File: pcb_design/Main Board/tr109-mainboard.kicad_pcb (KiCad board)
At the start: 2 copper layers, 60.3 x 60.4 mm, 23 parts, among them J1 Raspberry Pi Zero W, J2 ST7735_Screen, J3 Light_Board, J4 Cap_and_Bat, J5 Hall_1, J6 Audio_Out, J7 Hall_2, J8 Led_On, J9 i2c Connect, U1 CAP1208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

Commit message: Updated PCBs
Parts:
- added G***: Picorder Logo, Logos:Picorder Logo, F.Cu at (150.9, 101.0)
- J2: value ST7735_Screen -> ST7735 Screen
- moved J9 10.2 mm to (164.8, 110.9)
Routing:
- net SDA: track 94.4 -> 104.5 mm
- net SCL: track 90.5 -> 99.1 mm
- net 3v3: track 98.5 -> 106.2 mm
- net LED_ON: track 75.2 -> 76.4 mm
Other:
- board text added: "C.BARRETT 2025"
- board text added: "CAPACITIVE PADS"
- board text added: "GNDN"
- board text added: "H2"
- board text added: "HALL SENSOR 2"
- board text added: "STATUS"
- board text removed: "CAPACITIVE BUTTONS"
- board text removed: "GNDN 47"
- board text removed: "LOW"

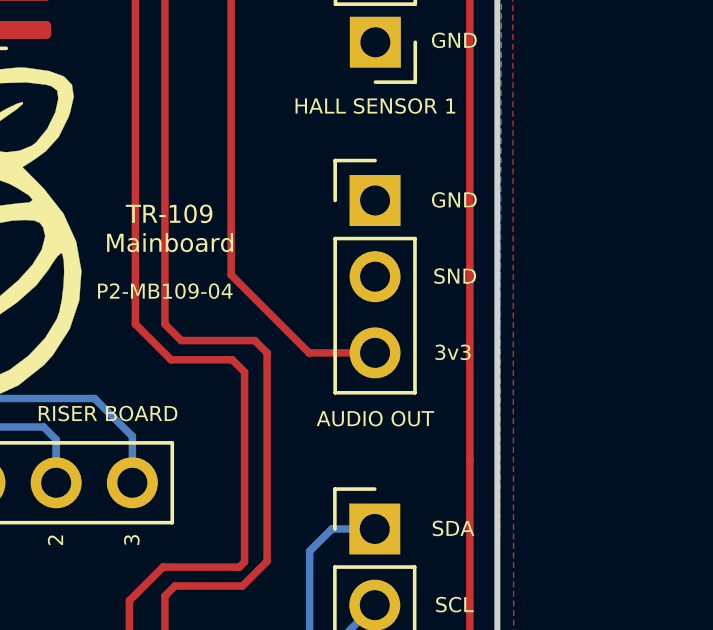
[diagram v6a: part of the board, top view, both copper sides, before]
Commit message: Fixed some kicad PCB errors, updated Blender file
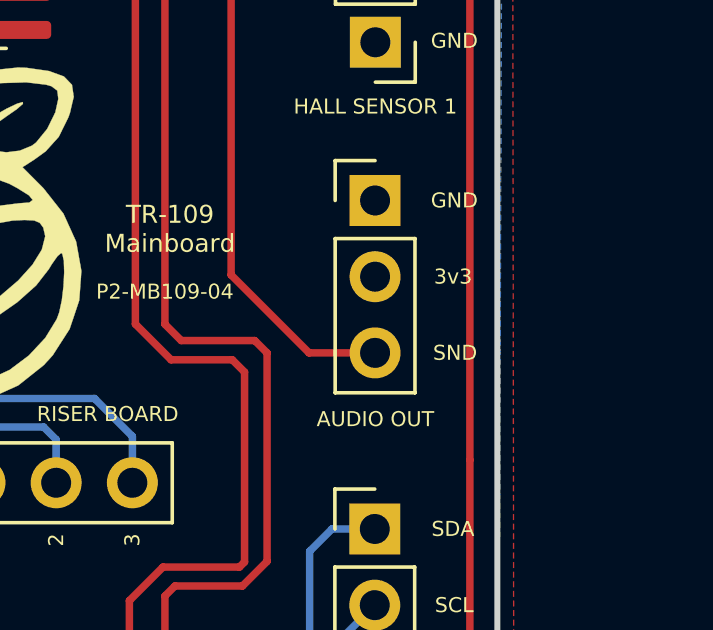
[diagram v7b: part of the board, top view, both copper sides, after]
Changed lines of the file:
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@@
 	)
 	(gr_text "SND"
-		(at 161.7356 102.4794 -0)
+		(at 161.7356 105.0194 -0)
 		(layer "B.SilkS")
 		(effects
@@
 	)
 	(gr_text "3v3"
-		(at 161.902268 105.0194 -0)
+		(at 161.902268 102.4794 -0)
 		(layer "B.SilkS")
 		(effects
@@
 	)
 	(gr_text "SND"
-		(at 168.246435 102.4794 0)
+		(at 168.246435 105.0194 0)
 		(layer "F.SilkS")
 		(effects
@@
 	)
 	(gr_text "3v3"
-		(at 168.079767 105.0194 0)
-		(layer "F.SilkS")
-		(effects
+		(at 168.079767 102.4794 0)
+		(layer "F.SilkS")
+		(effects
